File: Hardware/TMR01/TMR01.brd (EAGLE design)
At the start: 41 x 45.7 mm, 36 parts, among them U1 ATMEGA328P_TQFP, U2 DS3234

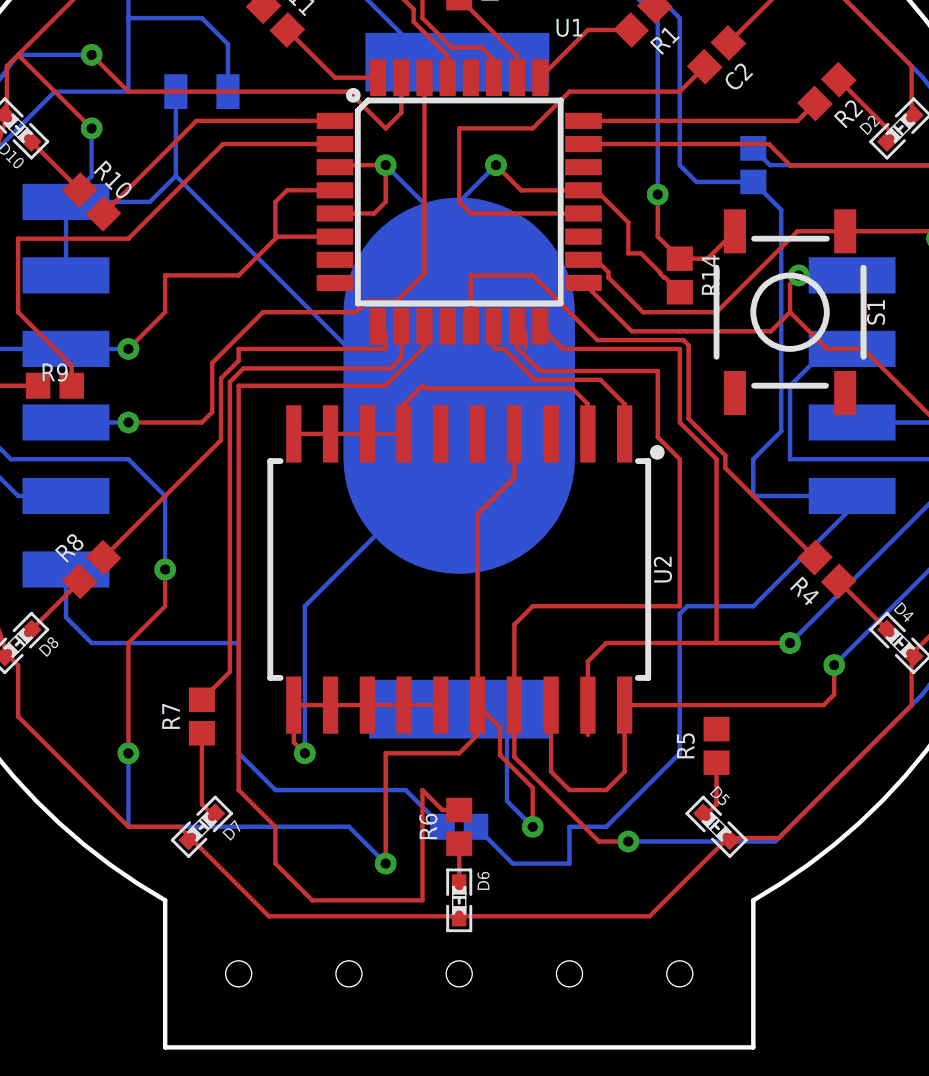
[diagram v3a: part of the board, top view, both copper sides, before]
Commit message: Ratsnest – Nothing To Do!
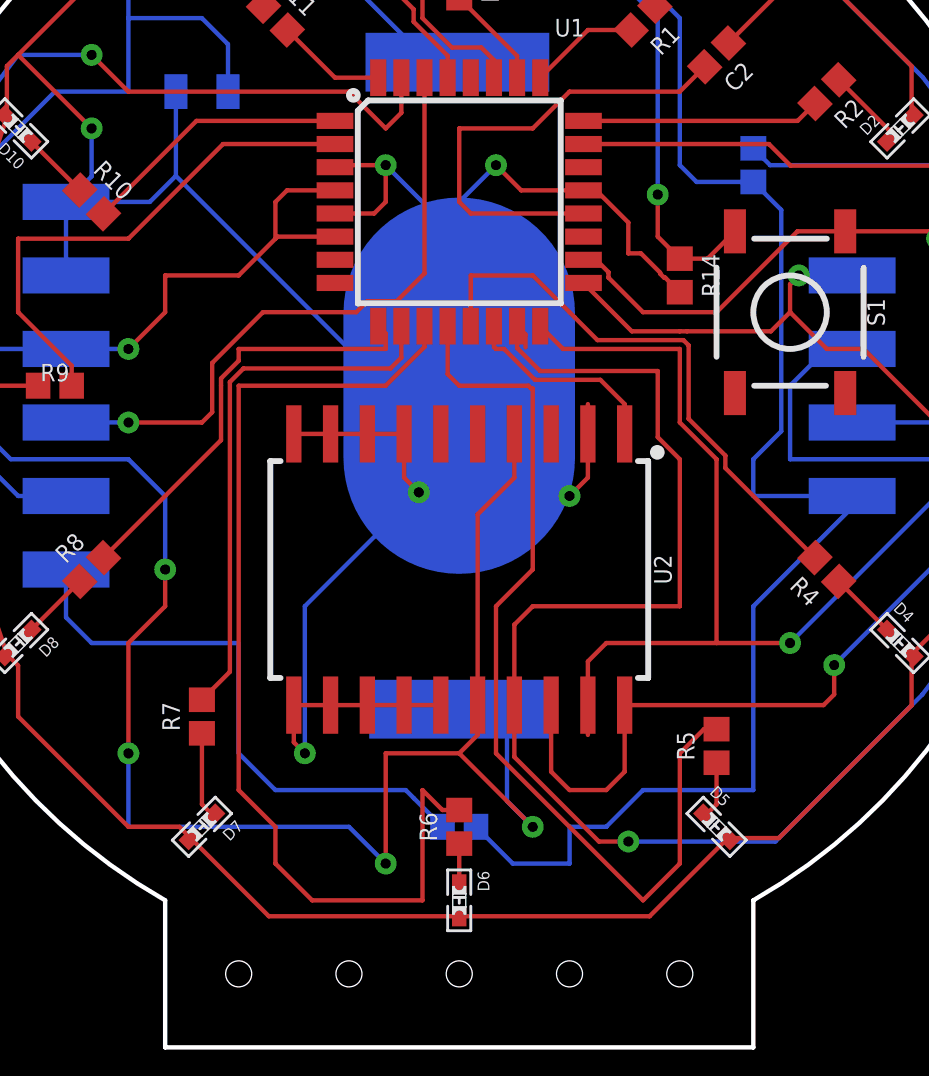
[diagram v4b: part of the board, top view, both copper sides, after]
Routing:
- net D7: track 0.00 -> 32.3 mm
- net GND: track 204.3 -> 206.0 mm, vias 4 -> 6
- net VCC: track 173.7 -> 172.3 mm
- net RST: track 65.8 -> 66.7 mm
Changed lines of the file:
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@@
 <wire x1="22.225" y1="26.275" x2="23.495" y2="26.275" width="0.1524" layer="1"/>
 <wire x1="31.115" y1="26.275" x2="31.115" y2="27.305" width="0.1524" layer="1"/>
-<wire x1="31.115" y1="27.305" x2="30.5816" y2="27.8384" width="0.1524" layer="1"/>
-<wire x1="25.4" y1="27.94" x2="25.5016" y2="27.8384" width="0.1524" layer="1"/>
-<wire x1="30.5816" y1="27.8384" x2="25.5016" y2="27.8384" width="0.1524" layer="1"/>
-<wire x1="24.765" y1="26.275" x2="24.765" y2="27.305" width="0.1524" layer="1"/>
-<wire x1="24.765" y1="27.305" x2="25.4" y2="27.94" width="0.1524" layer="1"/>
 <wire x1="16.88" y1="38.1" x2="16.88" y2="35.19" width="0.1524" layer="16"/>
-<wire x1="16.88" y1="35.19" x2="24.13" y2="27.94" width="0.1524" layer="16"/>
-<wire x1="24.13" y1="27.94" x2="26.416" y2="27.94" width="0.1524" layer="16"/>
+<wire x1="24.13" y1="27.94" x2="16.88" y2="35.19" width="0.1524" layer="16"/>
 <wire x1="26.416" y1="27.94" x2="26.67" y2="27.94" width="0.1524" layer="16"/>
 <wire x1="13.085" y1="31.75" x2="13.085" y2="34.29" width="0.1524" layer="16"/>
@@
 <via x="21.336" y="15.24" extent="1-16" drill="0.35"/>
 <wire x1="21.336" y1="15.24" x2="21.336" y2="20.32" width="0.1524" layer="16"/>
-<wire x1="21.336" y1="20.32" x2="26.416" y2="25.4" width="0.1524" layer="16"/>
+<wire x1="21.336" y1="20.32" x2="25.273" y2="24.257" width="0.1524" layer="16"/>
+<wire x1="25.273" y1="24.257" x2="26.416" y2="25.4" width="0.1524" layer="16"/>
 <wire x1="26.416" y1="25.4" x2="26.416" y2="27.94" width="0.1524" layer="16"/>
 <wire x1="22.3774" y1="33.89" x2="23.73" y2="33.89" width="0.1524" layer="1"/>
@@
 <via x="24.13" y="35.56" extent="1-16" drill="0.35"/>
 <wire x1="24.13" y1="35.56" x2="26.67" y2="33.02" width="0.1524" layer="16"/>
-<wire x1="26.67" y1="33.02" x2="26.67" y2="30.48" width="0.1524" layer="16"/>
-<wire x1="26.67" y1="30.48" x2="26.67" y2="27.94" width="0.1524" layer="16"/>
+<wire x1="26.67" y1="33.02" x2="26.67" y2="27.94" width="0.1524" layer="16"/>
 <wire x1="30.9626" y1="34.69" x2="28.81" y2="34.69" width="0.1524" layer="1"/>
 <wire x1="28.81" y1="34.69" x2="27.94" y2="35.56" width="0.1524" layer="1"/>
@@
 <wire x1="27.94" y1="35.56" x2="26.67" y2="34.29" width="0.1524" layer="16"/>
 <wire x1="26.67" y1="34.29" x2="26.67" y2="33.02" width="0.1524" layer="16"/>
-<wire x1="26.416" y1="27.94" x2="25.5016" y2="27.8384" width="0" layer="19" extent="1-16"/>
+<wire x1="31.115" y1="26.275" x2="31.115" y2="24.765" width="0.1524" layer="1"/>
+<wire x1="31.115" y1="24.765" x2="30.48" y2="24.13" width="0.1524" layer="1"/>
+<via x="30.48" y="24.13" extent="1-16" drill="0.35"/>
+<wire x1="30.48" y1="24.13" x2="27.686" y2="24.13" width="0.1524" layer="16"/>
+<wire x1="27.686" y1="24.13" x2="26.416" y2="25.4" width="0.1524" layer="16"/>
+<wire x1="24.765" y1="26.275" x2="24.765" y2="24.765" width="0.1524" layer="1"/>
+<wire x1="24.765" y1="24.765" x2="25.273" y2="24.257" width="0.1524" layer="1"/>
+<wire x1="25.4" y1="24.13" x2="25.273" y2="24.257" width="0.1524" layer="1"/>
+<via x="25.273" y="24.257" extent="1-16" drill="0.35"/>
+<wire x1="26.67" y1="27.94" x2="24.13" y2="27.94" width="0.1524" layer="16"/>
 </signal>
 <signal name="VCC">
@@
 <wire x1="27.305" y1="23.495" x2="27.305" y2="16.905" width="0.1524" layer="1"/>
 <wire x1="28.575" y1="24.765" x2="27.305" y2="23.495" width="0.1524" layer="1"/>
-<wire x1="27.305" y1="16.905" x2="28.0814" y2="16.1286" width="0.1524" layer="1"/>
-<wire x1="28.0814" y1="16.1286" x2="28.0814" y2="15.17554375" width="0.1524" layer="1"/>
-<wire x1="28.0814" y1="15.17554375" x2="29.21" y2="14.04694375" width="0.1524" layer="1"/>
 <via x="29.21" y="12.7" extent="1-16" drill="0.35"/>
 <wire x1="29.21" y1="12.7" x2="28.321" y2="13.589" width="0.1524" layer="16"/>
 <wire x1="28.321" y1="13.589" x2="28.321" y2="16.764" width="0.1524" layer="16"/>
-<wire x1="29.21" y1="14.04694375" x2="29.21" y2="12.7" width="0.1524" layer="1"/>
 <wire x1="28.321" y1="16.764" x2="25.146" y2="16.764" width="0.1524" layer="16"/>
 <wire x1="27.305" y1="16.905" x2="27.305" y2="15.875" width="0.1524" layer="1"/>
@@
 <wire x1="15.24" y1="25.4" x2="11.176" y2="25.4" width="0.1524" layer="16"/>
 <wire x1="10.668" y1="25.908" x2="10.668" y2="29.21" width="0.1524" layer="16"/>
+<wire x1="29.21" y1="12.7" x2="26.67" y2="15.24" width="0.1524" layer="1"/>
 </signal>
 <signal name="RST">
@@
 <contactref element="C1" pad="2"/>
 <contactref element="R13" pad="2"/>
-<wire x1="34.544" y1="20.32" x2="36.83" y2="20.32" width="0.1524" layer="16"/>
 <contactref element="J2" pad="1"/>
 <wire x1="36.83" y1="20.32" x2="40.245" y2="23.735" width="0.1524" layer="16"/>
@@
 <wire x1="30.48" y1="11.43" x2="30.48" y2="12.7" width="0.1524" layer="16"/>
 <wire x1="30.48" y1="12.7" x2="31.75" y2="12.7" width="0.1524" layer="16"/>
-<wire x1="31.75" y1="12.7" x2="34.29" y2="15.24" width="0.1524" layer="16"/>
-<wire x1="34.29" y1="15.24" x2="34.29" y2="20.066" width="0.1524" layer="16"/>
-<wire x1="34.29" y1="20.066" x2="34.544" y2="20.32" width="0.1524" layer="16"/>
+<wire x1="31.75" y1="12.7" x2="33.02" y2="13.97" width="0.1524" layer="16"/>
+<wire x1="33.02" y1="13.97" x2="36.83" y2="13.97" width="0.1524" layer="16"/>
+<wire x1="36.83" y1="13.97" x2="36.83" y2="20.32" width="0.1524" layer="16"/>
 </signal>
 <signal name="DTR">
@@
 <contactref element="U1" pad="12"/>
 <contactref element="R5" pad="2"/>
-<wire x1="35.56" y1="16.074" x2="26.27" y2="29.9974" width="0" layer="19" extent="1-1"/>
+<wire x1="26.27" y1="29.9974" x2="26.27" y2="28.34" width="0.1524" layer="1"/>
+<wire x1="26.27" y1="28.34" x2="26.67" y2="27.94" width="0.1524" layer="1"/>
+<wire x1="26.67" y1="27.94" x2="29.05865625" y2="27.94" width="0.1524" layer="1"/>
+<wire x1="29.05865625" y1="27.94" x2="29.16025625" y2="27.8384" width="0.1524" layer="1"/>
+<wire x1="29.16025625" y1="27.8384" x2="29.21" y2="27.8384" width="0.1524" layer="1"/>
+<wire x1="29.21" y1="21.59" x2="27.94" y2="20.32" width="0.1524" layer="1"/>
+<wire x1="29.21" y1="27.8384" x2="29.21" y2="21.59" width="0.1524" layer="1"/>
+<wire x1="33.02" y1="10.16" x2="34.29" y2="11.43" width="0.1524" layer="1"/>
+<wire x1="34.29" y1="11.43" x2="34.29" y2="15.24" width="0.1524" layer="1"/>
+<wire x1="34.29" y1="15.24" x2="35.124" y2="16.074" width="0.1524" layer="1"/>
+<wire x1="35.124" y1="16.074" x2="35.56" y2="16.074" width="0.1524" layer="1"/>
+<wire x1="27.94" y1="20.32" x2="27.94" y2="15.24" width="0.1524" layer="1"/>
+<wire x1="27.94" y1="15.24" x2="33.02" y2="10.16" width="0.1524" layer="1"/>
 </signal>
 <signal name="MISO">

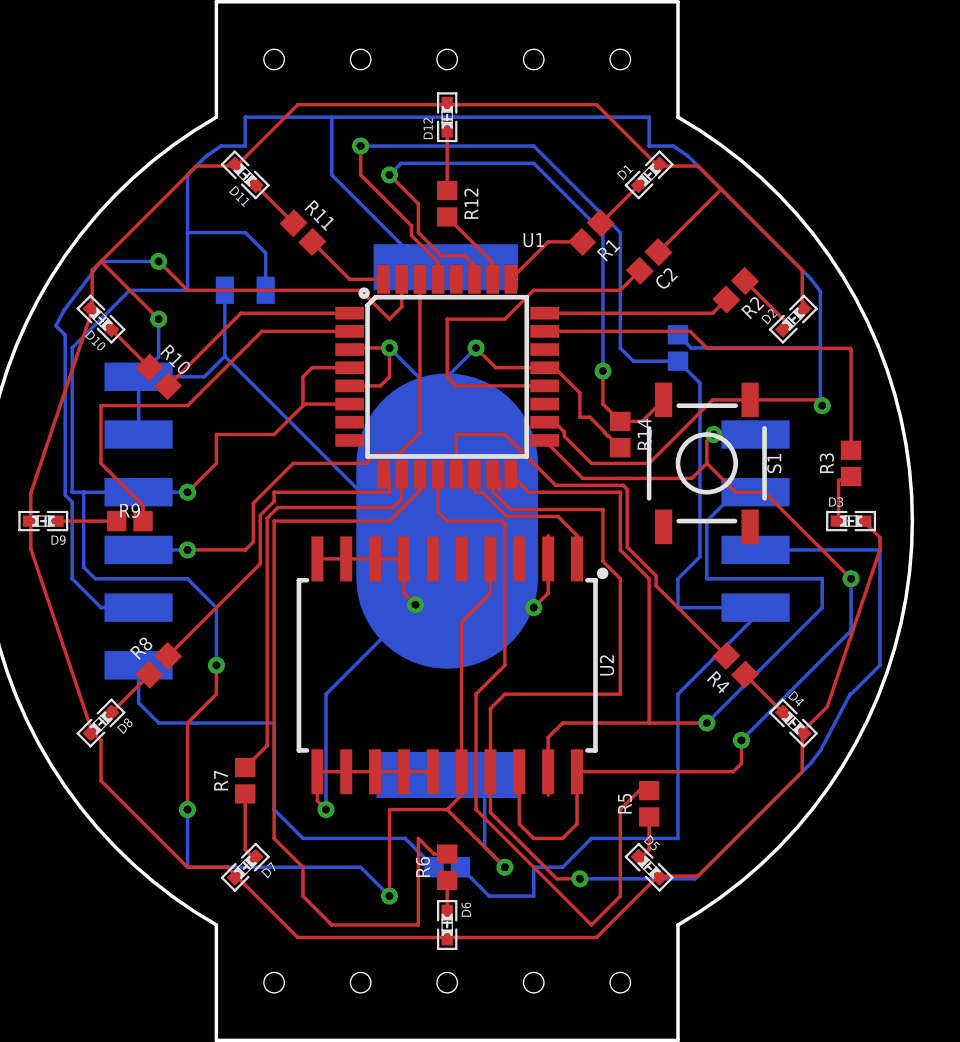
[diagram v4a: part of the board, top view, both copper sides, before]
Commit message: HW after route evertything and having 300 errors. Looking for another solution
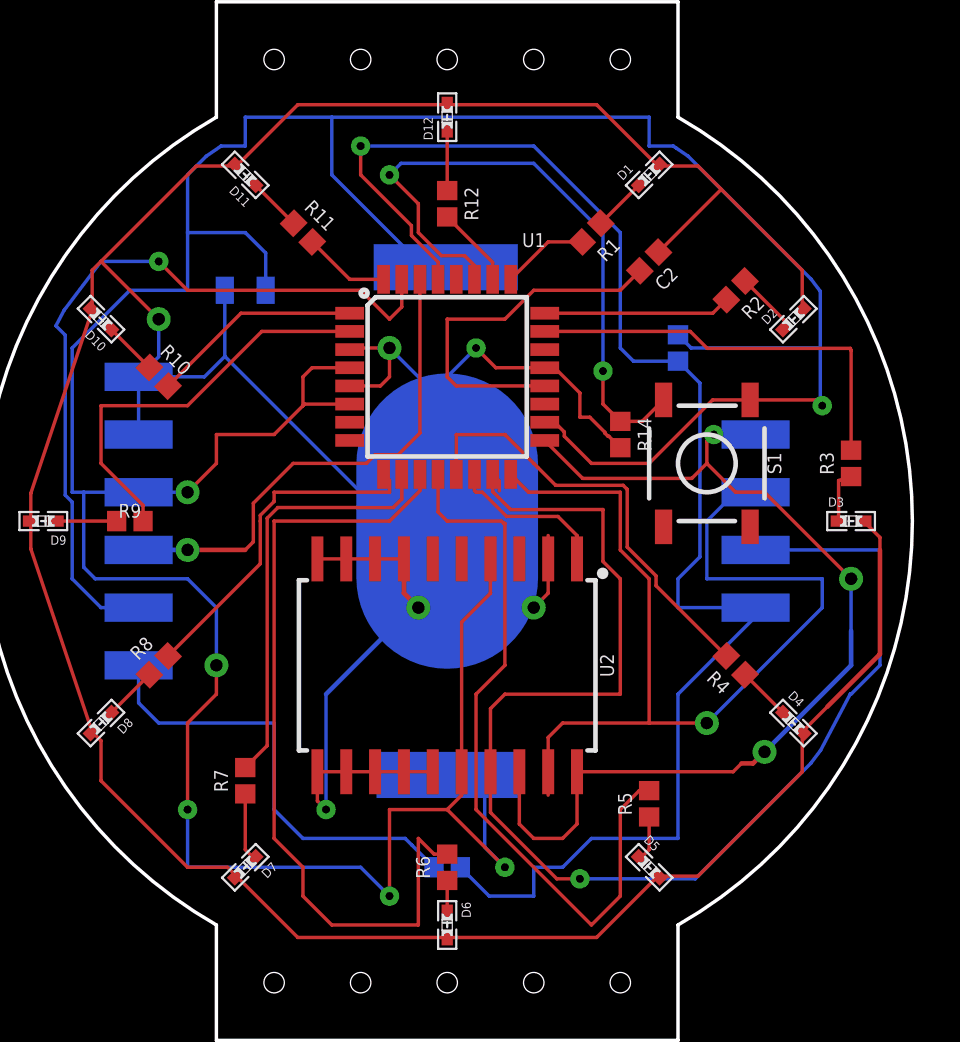
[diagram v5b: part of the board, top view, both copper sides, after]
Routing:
- net GND: track 206.0 -> 209.3 mm
